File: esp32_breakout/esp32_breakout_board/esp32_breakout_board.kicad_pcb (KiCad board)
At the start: 2 copper layers, 26.4 x 31.8 mm, 7 parts, among them U4 ESP32-S3-MINI-1

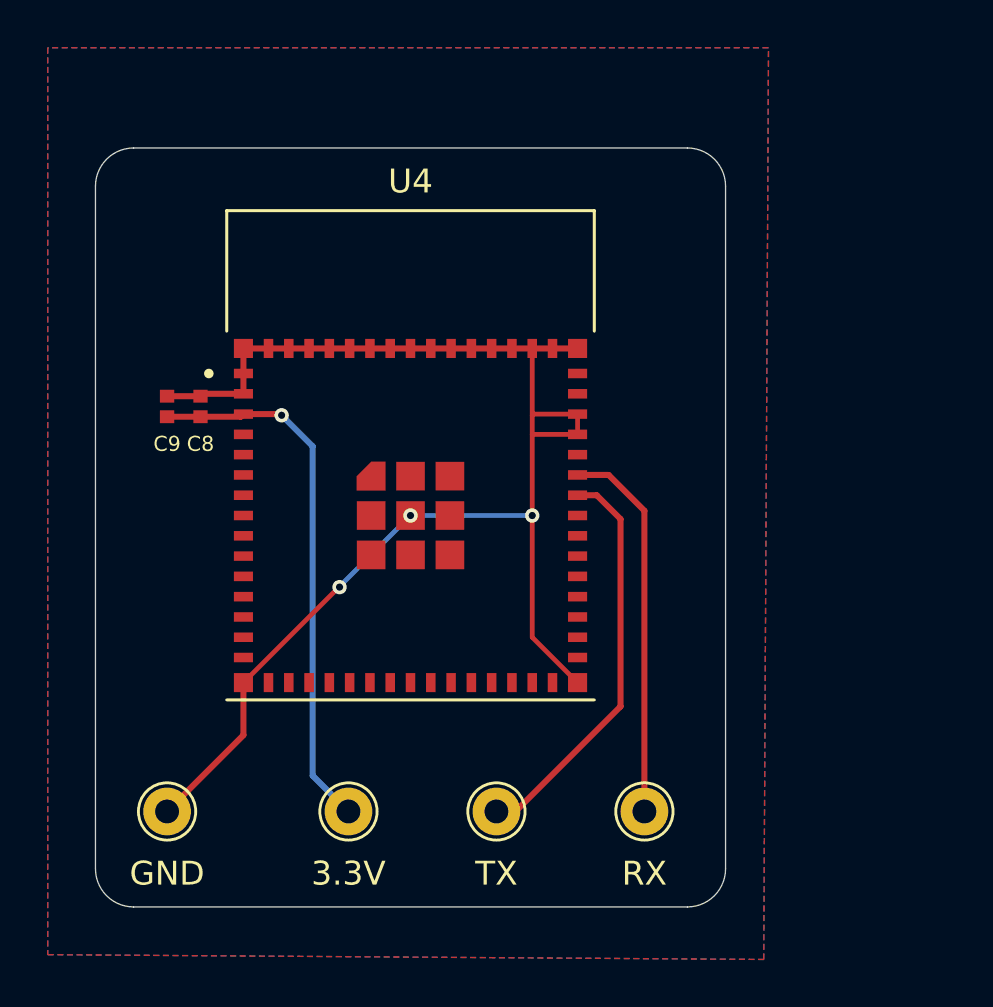
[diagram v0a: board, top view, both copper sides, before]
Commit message: Included resistors for EN/GPIO0 on ESP32
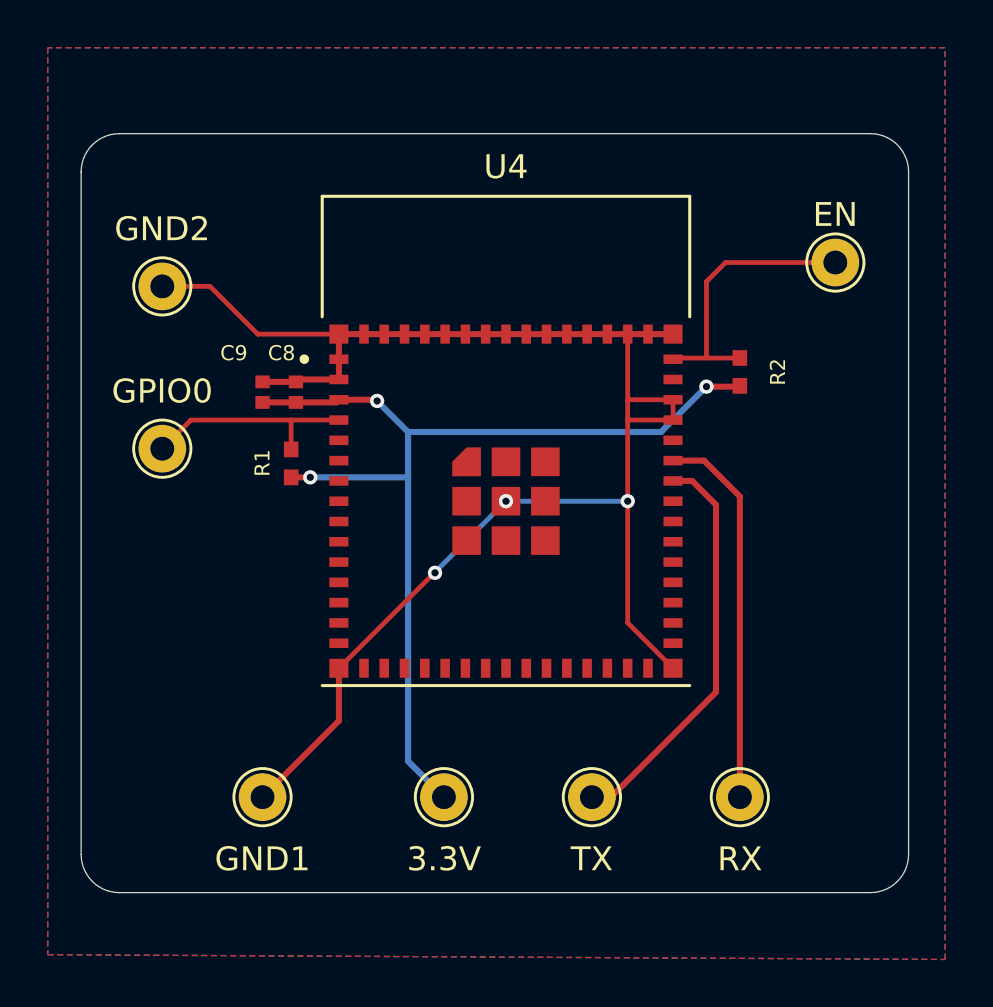
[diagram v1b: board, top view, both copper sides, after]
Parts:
- added EN: TestPoint, TestPoint:TestPoint_THTPad_D2.0mm_Drill1.0mm, F.Cu at (147.0, 73.0)
- added GND2: TestPoint, TestPoint:TestPoint_THTPad_D2.0mm_Drill1.0mm, F.Cu at (118.8, 74.0)
- added GPIO0: TestPoint, TestPoint:TestPoint_THTPad_D2.0mm_Drill1.0mm, F.Cu at (118.8, 80.8)
- added R1: 10k, RC0402FR-7D4K7L:RESC1005X40N, F.Cu at (124.2, 81.4)
- added R2: 10k, RC0402FR-7D4K7L:RESC1005X40N, F.Cu at (143.0, 77.6)
- moved 3.3V 4.04 mm to (130.6, 95.4)
- moved C8 4.04 mm to (124.4, 78.4)
- moved C9 4.04 mm to (123.0, 78.4)
- moved GND1 4.04 mm to (123.0, 95.4)
- moved RX 4.04 mm to (143.0, 95.4)
- moved TX 4.04 mm to (136.8, 95.4)
- moved U4 4.04 mm to (133.2, 83.0)
- renumbered GND to GND1
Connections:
- U4 pad 4: unconnected-(U4-IO0-Pad4) -> GPIO0
- U4 pad 45: unconnected-(U4-EN-Pad45) -> EN
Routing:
- net +3.3V: track 22.6 -> 42.2 mm, vias 1 -> 3
- net EN: track 0.00 -> 11.8 mm
- net GPIO0: track 0.00 -> 9.13 mm
- net GND: track 60.5 -> 68.7 mm
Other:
- board size 26.4 x 31.8 mm -> 34.7 x 31.8 mm
